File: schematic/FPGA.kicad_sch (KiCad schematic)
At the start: 0 parts

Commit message: Create FPGA schematic
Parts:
- added C5: 10uF, Capacitor_SMD:C_0603_1608Metric, symbol Device:C
- added C6: 100nF, Capacitor_SMD:C_0603_1608Metric, symbol Device:C
- added D2: D, Diode_SMD:D_0603_1608Metric, symbol Device:D
- added J2: Flash, Connector_PinHeader_2.54mm:PinHeader_1x06_P2.54mm_Vertical, symbol Connector:Conn_01x06_Pin
- added J3: SPI Select, Connector_PinHeader_2.54mm:PinHeader_1x02_P2.54mm_Vertical, symbol Connector:Conn_01x02_Pin
- added R2: 470R, Resistor_SMD:R_0603_1608Metric, symbol Device:R
- added R3, R4, R5, R6, R7, R8, R9: 10k, Resistor_SMD:R_0603_1608Metric, symbol Device:R
- added U3: ICE5LP1K-SG48ITR, ICE5LP1K-SG48ITR:QFN50P700X700X100-49N, symbol iCE5LP1K:ICE5LP1K-SG48ITR
- added U4: AT25DN011-SSHF-T, AT25DN011-SSHF-T:SOIC127P599X175-8N, symbol AT25DN011:AT25DN011-SSHF-T
- added U5: CCBTLV3257MPWREP, CCBTLV3257MPWREP:SOP65P640X120-16N, symbol CCBTLV3257:CCBTLV3257MPWREP
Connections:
- new net: J2.1 (Pin_1), R3.2, U3.7 (CDONE)
- new net: J3.1 (Pin_1), R9.2, U5.1 (S)
- new net: C5.1, C6.1, R2.2, U3.29 (VCCPLL)
- new net: J2.2 (Pin_2), R4.2, U3.8 (CRESET_B)
- new net: R7.2, U4.3 (~{WP})
- new net: R8.2, U4.7 (~{HOLD})
- new net: D2.1 (K), U3.24 (VPP_2V5)
- new net +1V2: R2.1, U3.30 (VCC), U3.5 (VCC)
- new net +3V3: D2.2 (A), R3.1, R4.1, R5.1, R6.1, R7.1, R8.1, R9.1, U3.1 (VCCIO_2), U3.22 (SPI_VCCIO1), U3.33 (VCCIO_0), U4.8 (VCC), U5.16 (VCC)
- new net CONN_SPI_CS: J2.6 (Pin_6), U5.14 (4B1)
- new net CONN_SPI_SCK: J2.5 (Pin_5), U5.11 (3B1)
- new net CONN_SPI_SI: J2.4 (Pin_4), U5.5 (2B1)
- new net CONN_SPI_SO: J2.3 (Pin_3), U5.2 (1B1)
- new net FLASH_SPI_CS: U4.1 (~{CS}), U5.12 (4A)
- new net FLASH_SPI_SCK: U4.6 (SCK), U5.9 (3A)
- new net FLASH_SPI_SI: U4.5 (SI(I/O0)), U5.7 (2A)
- new net FLASH_SPI_SO: U4.2 (SO(I/O1)), U5.4 (1A)
- new net FPGA_SPI_CS: R6.2, U3.16 (IOB_35B_SPI_CSN), U5.13 (4B2)
- new net FPGA_SPI_SCK: R5.2, U3.15 (IOB_34A_SPI_SCK), U5.10 (3B2)
- new net FPGA_SPI_SI: U3.14 (IOB_32A_SPI_SO), U5.6 (2B2)
- new net FPGA_SPI_SO: U3.17 (IOB_33B_SPI_SI), U5.3 (1B2)
- new net GND: C5.2, C6.2, J3.2 (Pin_2), U3.49 (GND), U4.4 (GND), U5.15 (~{OE}), U5.8 (GND)
- new net IO0: U3.46 (IOB_0A)
- new net IO13: U3.6 (IOB_13B)
- new net IO16: U3.9 (IOB_16A)
- new net IO18: U3.10 (IOB_18A)
- new net IO2: U3.47 (IOB_2A)
- new net IO20: U3.11 (IOB_20A)
- new net IO22: U3.12 (IOB_22A)
- new net IO23: U3.21 (IOB_23B)
- new net IO24: U3.13 (IOB_24A)
- new net IO25: U3.20 (IOB_25B_G3)
- new net IO29: U3.19 (IOB_29B)
- new net IO3: U3.44 (IOB_3B_G6)
- new net IO31: U3.18 (IOB_31B)
- new net IO36: U3.25 (IOT_36B)
- new net IO37: U3.23 (IOT_37A)
- new net IO38: U3.27 (IOT_38B)
- new net IO39: U3.26 (IOT_39A)
- new net IO4: U3.48 (IOB_4A)
- new net IO41: U3.28 (IOT_41A)
- new net IO42: U3.31 (IOT_42B)
- new net IO43: U3.32 (IOT_43A)
- new net IO44: U3.34 (IOT_44B)
- new net IO45: U3.37 (IOT_45A_G1)
- new net IO46: U3.35 (IOT_46B_G0)
- new net IO48: U3.36 (IOT_48B)
- new net IO49: U3.43 (IOT_49A)
- new net IO5: U3.45 (IOB_5B)
- new net IO50: U3.38 (IOT_50B)
- new net IO51: U3.42 (IOT_51A)
- new net IO6: U3.2 (IOB_6A)
- new net IO8: U3.4 (IOB_8A)
- new net IO9: U3.3 (IOB_9B)
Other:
- title: (none) -> iCE40 DevBoard

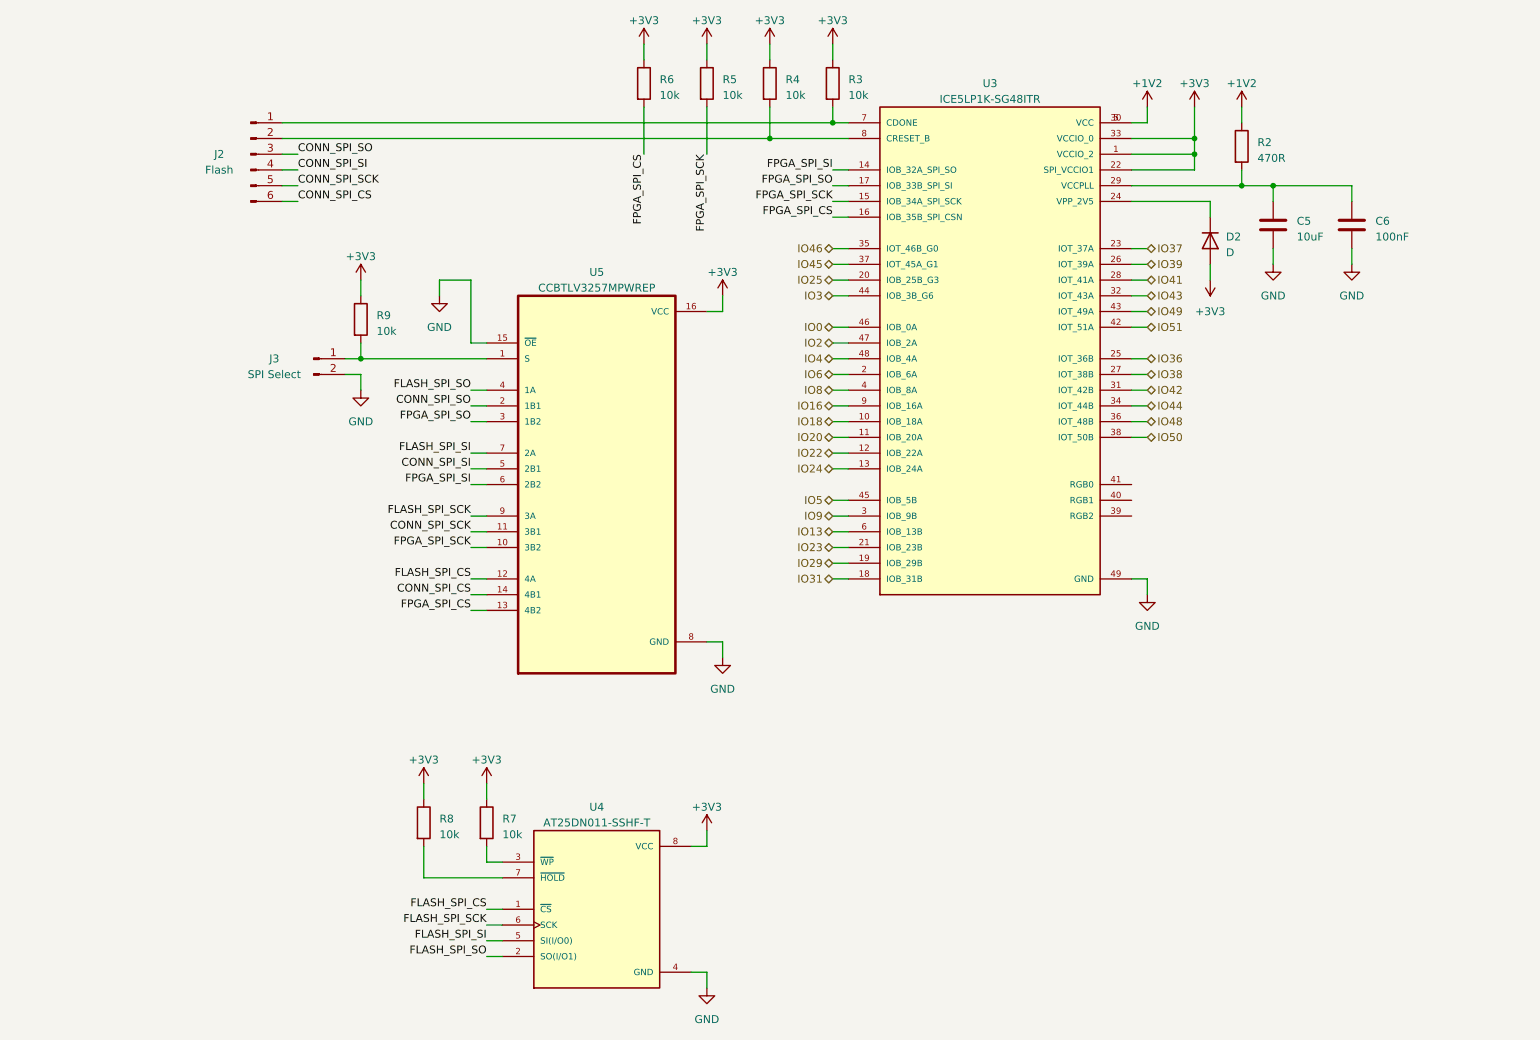
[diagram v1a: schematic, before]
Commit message: Add level shifters to SPI lines
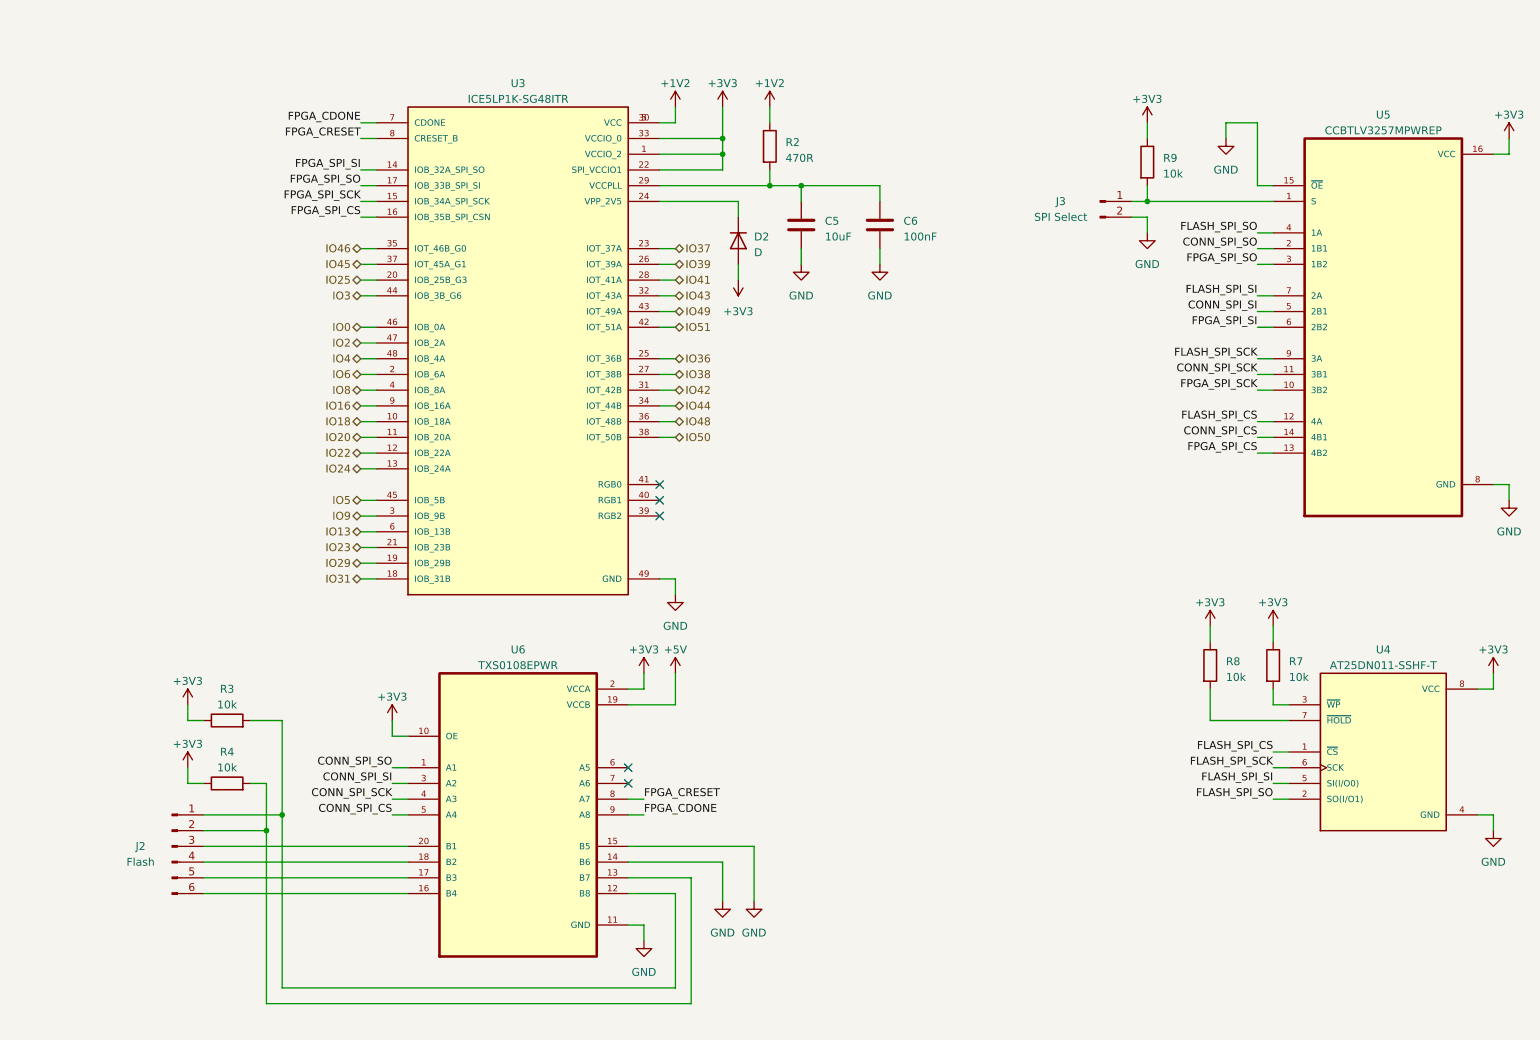
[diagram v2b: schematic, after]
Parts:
- removed R5, R6: 10k, Resistor_SMD:R_0603_1608Metric, symbol Device:R
- added U6: TXS0108EPWR, TXS0108EPWR:SOP65P640X120-20N, symbol TXS0108EPWR:TXS0108EPWR
- R3, R4: footprint Resistor_SMD:R_0603_1608Metric -> (none)
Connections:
- net +3V3: now also U6.10 (OE), U6.2 (VCCA)
- net CONN_SPI_CS: now also U6.5 (A4); no longer J2.6 (Pin_6)
- net CONN_SPI_SCK: now also U6.4 (A3); no longer J2.5 (Pin_5)
- net CONN_SPI_SI: now also U6.3 (A2); no longer J2.4 (Pin_4)
- net CONN_SPI_SO: now also U6.1 (A1); no longer J2.3 (Pin_3)
- net GND: now also U6.11 (GND), U6.14 (B6), U6.15 (B5)
- net at J2.1 (Pin_1), R3.2: now also U6.12 (B8); no longer U3.7 (CDONE)
- net at J2.2 (Pin_2), R4.2: now also U6.13 (B7); no longer U3.8 (CRESET_B)
- new net: J2.3 (Pin_3), U6.20 (B1)
- new net: J2.4 (Pin_4), U6.18 (B2)
- new net: J2.5 (Pin_5), U6.17 (B3)
- new net: J2.6 (Pin_6), U6.16 (B4)
- new net +5V: U6.19 (VCCB)
- new net FPGA_CDONE: U3.7 (CDONE), U6.9 (A8)
- new net FPGA_CRESET: U3.8 (CRESET_B), U6.8 (A7)
- no-connect marks 0 -> 5
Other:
- moved on the sheet: C5, C6, D2, J2, J3, R2, R7, R8, R9, U3, U4, U5

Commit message: Add testpoints to SPI lines
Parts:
- added TP10: FLASH_CS, TestPoint:TestPoint_Pad_D2.0mm, symbol Connector:TestPoint
- added TP11: FLASH_SCK, TestPoint:TestPoint_Pad_D2.0mm, symbol Connector:TestPoint
- added TP12: FLASH_SI, TestPoint:TestPoint_Pad_D2.0mm, symbol Connector:TestPoint
- added TP13: FLASH_SO, TestPoint:TestPoint_Pad_D2.0mm, symbol Connector:TestPoint
- added TP4: CDONE, TestPoint:TestPoint_Pad_D2.0mm, symbol Connector:TestPoint
- added TP5: CRESET, TestPoint:TestPoint_Pad_D2.0mm, symbol Connector:TestPoint
- added TP6: FPGA_SI, TestPoint:TestPoint_Pad_D2.0mm, symbol Connector:TestPoint
- added TP7: FPGA_SO, TestPoint:TestPoint_Pad_D2.0mm, symbol Connector:TestPoint
- added TP8: FPGA_SCK, TestPoint:TestPoint_Pad_D2.0mm, symbol Connector:TestPoint
- added TP9: FPGA_CS, TestPoint:TestPoint_Pad_D2.0mm, symbol Connector:TestPoint
- R3, R4: footprint (none) -> Resistor_SMD:R_0603_1608Metric
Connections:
- net FLASH_SPI_CS: now also TP10.1
- net FLASH_SPI_SCK: now also TP11.1
- net FLASH_SPI_SI: now also TP12.1
- net FLASH_SPI_SO: now also TP13.1
- net FPGA_CDONE: now also TP4.1
- net FPGA_CRESET: now also TP5.1
- net FPGA_SPI_CS: now also TP9.1
- net FPGA_SPI_SCK: now also TP8.1
- net FPGA_SPI_SI: now also TP6.1
- net FPGA_SPI_SO: now also TP7.1

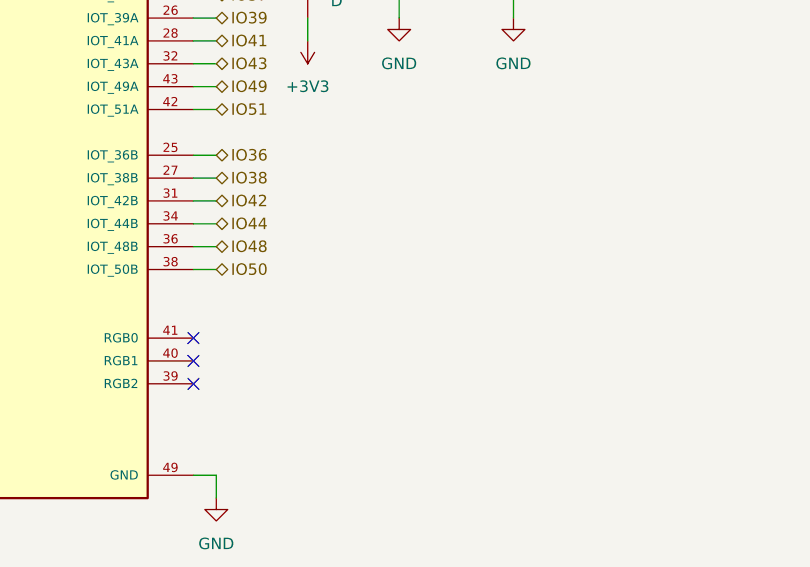
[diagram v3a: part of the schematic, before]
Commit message: Add RGB LEDs to schematic
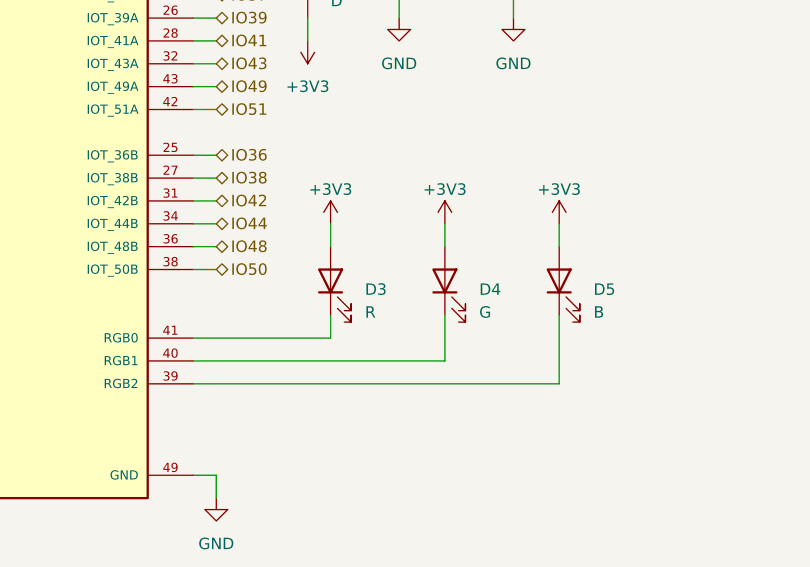
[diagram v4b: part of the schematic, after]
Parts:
- added D3: R, LED_SMD:LED_0805_2012Metric, symbol Device:LED
- added D4: G, LED_SMD:LED_0805_2012Metric, symbol Device:LED
- added D5: B, LED_SMD:LED_0805_2012Metric, symbol Device:LED
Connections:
- net +3V3: now also D3.2 (A), D4.2 (A), D5.2 (A)
- net at U3.39 (RGB2): now also D5.1 (K)
- net at U3.40 (RGB1): now also D4.1 (K)
- net at U3.41 (RGB0): now also D3.1 (K)
- no-connect marks 5 -> 2
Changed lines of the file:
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@@
   )
   (no_connect (at 119.38 142.24))
-  (no_connect (at 124.46 101.6))
-  (no_connect (at 124.46 96.52))
-  (no_connect (at 124.46 99.06))
   (no_connect (at 119.38 144.78))
   (wire (pts (xy 76.2 104.14) (xy 78.74 104.14))
@@
     (stroke (width 0) (type default))
   )
+  (wire (pts (xy 139.7 83.82) (xy 139.7 86.36))
+    (stroke (width 0) (type default))
+  )
   (wire (pts (xy 259.08 149.86) (xy 259.08 152.4))
     (stroke (width 0) (type default))
@@
     (stroke (width 0) (type default))
   )
+  (wire (pts (xy 124.46 96.52) (xy 139.7 96.52))
+    (stroke (width 0) (type default))
+  )
   (wire (pts (xy 48.26 144.78) (xy 50.8 144.78))
     (stroke (width 0) (type default))
   )
+  (wire (pts (xy 165.1 101.6) (xy 165.1 93.98))
+    (stroke (width 0) (type default))
+  )
   (wire (pts (xy 160.02 48.26) (xy 160.02 50.8))
     (stroke (width 0) (type default))
   )
+  (wire (pts (xy 165.1 83.82) (xy 165.1 86.36))
+    (stroke (width 0) (type default))
+  )
   (wire (pts (xy 119.38 154.94) (xy 139.7 154.94))
     (stroke (width 0) (type default))
@@
     (stroke (width 0) (type default))
   )
+  (wire (pts (xy 124.46 101.6) (xy 165.1 101.6))
+    (stroke (width 0) (type default))
+  )
   (wire (pts (xy 50.8 160.02) (xy 83.82 160.02))
     (stroke (width 0) (type default))
@@
     (stroke (width 0) (type default))
   )
+  (wire (pts (xy 152.4 99.06) (xy 152.4 93.98))
+    (stroke (width 0) (type default))
+  )
+  (wire (pts (xy 124.46 99.06) (xy 152.4 99.06))
+    (stroke (width 0) (type default))
+  )
   (wire (pts (xy 76.2 53.34) (xy 78.74 53.34))
     (stroke (width 0) (type default))
@@
     (stroke (width 0) (type default))
   )
+  (wire (pts (xy 139.7 96.52) (xy 139.7 93.98))
+    (stroke (width 0) (type default))
+  )
   (wire (pts (xy 76.2 66.04) (xy 78.74 66.04))
+    (stroke (width 0) (type default))
+  )
+  (wire (pts (xy 152.4 83.82) (xy 152.4 86.36))
     (stroke (width 0) (type default))
   )
@@
     (effects (font (size 1.27 1.27)) (justify right))
   )
+  (symbol (lib_id "power:+3V3") (at 152.4 83.82 0) (unit 1)
+    (in_bom yes) (on_board yes) (dnp no) (fields_autoplaced)
+    (property "Reference" "#PWR040" (at 152.4 87.63 0)
+      (effects (font (size 1.27 1.27)) hide)
+    )
+    (property "Value" "+3V3" (at 152.4 80.01 0)
+      (effects (font (size 1.27 1.27)))
+    )
+    (property "Footprint" "" (at 152.4 83.82 0)
+      (effects (font (size 1.27 1.27)) hide)
+    )
+    (property "Datasheet" "" (at 152.4 83.82 0)
+      (effects (font (size 1.27 1.27)) hide)
+    )
+    (pin "1")
+    (instances
+      (project "iCE40DevBoard"
+        (path "/2f10ad52-4a2c-425a-8339-df6126e31315/bb86ed21-cf66-42fc-a22b-eac1a192ec1e"
+          (reference "#PWR040") (unit 1)
+        )
+      )
+    )
+  )
   (symbol (lib_id "Device:R") (at 54.61 144.78 90) (unit 1)
     (in_bom yes) (on_board yes) (dnp no) (fields_autoplaced)
@@
         (path "/2f10ad52-4a2c-425a-8339-df6126e31315/bb86ed21-cf66-42fc-a22b-eac1a192ec1e"
           (reference "#PWR037") (unit 1)
+        )
+      )
+    )
+  )
+  (symbol (lib_id "Device:LED") (at 139.7 90.17 90) (unit 1)
+    (in_bom yes) (on_board yes) (dnp no) (fields_autoplaced)
+    (property "Reference" "D3" (at 143.51 91.1225 90)
+      (effects (font (size 1.27 1.27)) (justify right))
+    )
+    (property "Value" "R" (at 143.51 93.6625 90)
+      (effects (font (size 1.27 1.27)) (justify right))
+    )
+    (property "Footprint" "LED_SMD:LED_0805_2012Metric" (at 139.7 90.17 0)
+      (effects (font (size 1.27 1.27)) hide)
+    )
+    (property "Datasheet" "~" (at 139.7 90.17 0)
+      (effects (font (size 1.27 1.27)) hide)
+    )
+    (pin "1")
+    (pin "2")
+    (instances
+      (project "iCE40DevBoard"
+        (path "/2f10ad52-4a2c-425a-8339-df6126e31315/bb86ed21-cf66-42fc-a22b-eac1a192ec1e"
+          (reference "D3") (unit 1)
         )
       )
@@
     )
   )
+  (symbol (lib_id "Device:LED") (at 152.4 90.17 90) (unit 1)
+    (in_bom yes) (on_board yes) (dnp no) (fields_autoplaced)
+    (property "Reference" "D4" (at 156.21 91.1225 90)
+      (effects (font (size 1.27 1.27)) (justify right))
+    )
+    (property "Value" "G" (at 156.21 93.6625 90)
+      (effects (font (size 1.27 1.27)) (justify right))
+    )
+    (property "Footprint" "LED_SMD:LED_0805_2012Metric" (at 152.4 90.17 0)
+      (effects (font (size 1.27 1.27)) hide)
+    )
+    (property "Datasheet" "~" (at 152.4 90.17 0)
+      (effects (font (size 1.27 1.27)) hide)
+    )
+    (pin "1")
+    (pin "2")
+    (instances
+      (project "iCE40DevBoard"
+        (path "/2f10ad52-4a2c-425a-8339-df6126e31315/bb86ed21-cf66-42fc-a22b-eac1a192ec1e"
+          (reference "D4") (unit 1)
+        )
+      )
+    )
+  )
   (symbol (lib_id "Connector:TestPoint") (at 180.34 147.32 270) (unit 1)
     (in_bom yes) (on_board yes) (dnp no)
@@
     )
   )
+  (symbol (lib_id "power:+3V3") (at 139.7 83.82 0) (unit 1)
+    (in_bom yes) (on_board yes) (dnp no) (fields_autoplaced)
+    (property "Reference" "#PWR025" (at 139.7 87.63 0)
+      (effects (font (size 1.27 1.27)) hide)
+    )
+    (property "Value" "+3V3" (at 139.7 80.01 0)
+      (effects (font (size 1.27 1.27)))
+    )
+    (property "Footprint" "" (at 139.7 83.82 0)
+      (effects (font (size 1.27 1.27)) hide)
+    )
+    (property "Datasheet" "" (at 139.7 83.82 0)
+      (effects (font (size 1.27 1.27)) hide)
+    )
+    (pin "1")
+    (instances
+      (project "iCE40DevBoard"
+        (path "/2f10ad52-4a2c-425a-8339-df6126e31315/bb86ed21-cf66-42fc-a22b-eac1a192ec1e"
+          (reference "#PWR025") (unit 1)
+        )
+      )
+    )
+  )
   (symbol (lib_id "Device:R") (at 223.52 125.73 0) (unit 1)
     (in_bom yes) (on_board yes) (dnp no) (fields_autoplaced)
@@
         (path "/2f10ad52-4a2c-425a-8339-df6126e31315/bb86ed21-cf66-42fc-a22b-eac1a192ec1e"
           (reference "R7") (unit 1)
+        )
+      )
+    )
+  )
+  (symbol (lib_id "Device:LED") (at 165.1 90.17 90) (unit 1)
+    (in_bom yes) (on_board yes) (dnp no) (fields_autoplaced)
+    (property "Reference" "D5" (at 168.91 91.1225 90)
+      (effects (font (size 1.27 1.27)) (justify right))
+    )
+    (property "Value" "B" (at 168.91 93.6625 90)
+      (effects (font (size 1.27 1.27)) (justify right))
+    )
+    (property "Footprint" "LED_SMD:LED_0805_2012Metric" (at 165.1 90.17 0)
+      (effects (font (size 1.27 1.27)) hide)
+    )
+    (property "Datasheet" "~" (at 165.1 90.17 0)
+      (effects (font (size 1.27 1.27)) hide)
+    )
+    (pin "1")
+    (pin "2")
+    (instances
+      (project "iCE40DevBoard"
+        (path "/2f10ad52-4a2c-425a-8339-df6126e31315/bb86ed21-cf66-42fc-a22b-eac1a192ec1e"
+          (reference "D5") (unit 1)
         )
       )
@@
         )
       )
+    )
+  )
+  (symbol (lib_id "power:+3V3") (at 165.1 83.82 0) (unit 1)
+    (in_bom yes) (on_board yes) (dnp no) (fields_autoplaced)
+    (property "Reference" "#PWR041" (at 165.1 87.63 0)
+      (effects (font (size 1.27 1.27)) hide)
+    )
+    (property "Value" "+3V3" (at 165.1 80.01 0)
+      (effects (font (size 1.27 1.27)))
+    )
+    (property "Footprint" "" (at 165.1 83.82 0)
+      (effects (font (size 1.27 1.27)) hide)
+    )
+    (property "Datasheet" "" (at 165.1 83.82 0)
+      (effects (font (size 1.27 1.27)) hide)
+    )
+    (pin "1")
+    (instances
+      (project "iCE40DevBoard"
+        (path "/2f10ad52-4a2c-425a-8339-df6126e31315/bb86ed21-cf66-42fc-a22b-eac1a192ec1e"
+          (reference "#PWR041") (unit 1)
+        )
+      )
